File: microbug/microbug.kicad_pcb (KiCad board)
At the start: 2 copper layers, 32.5 x 39.1 mm, 18 parts, among them J1 Conn_01x03, J2 Conn_01x03, M1 Motor_DC, M2 Motor_DC, U1 ATtiny1616-S, U2 QRE1113GR, U3 TC78H651AFNG, U4 QRE1113GR

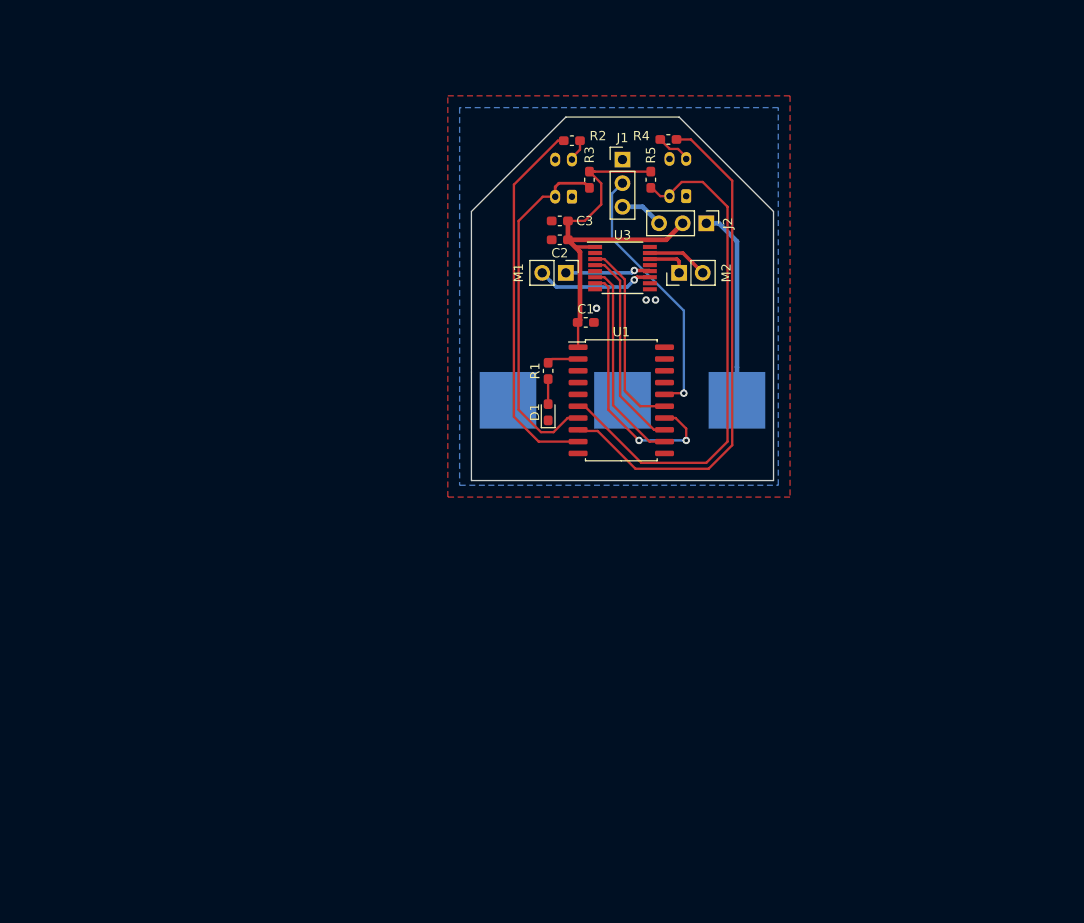
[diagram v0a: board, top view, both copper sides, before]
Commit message: Added more LEDs, changed outline
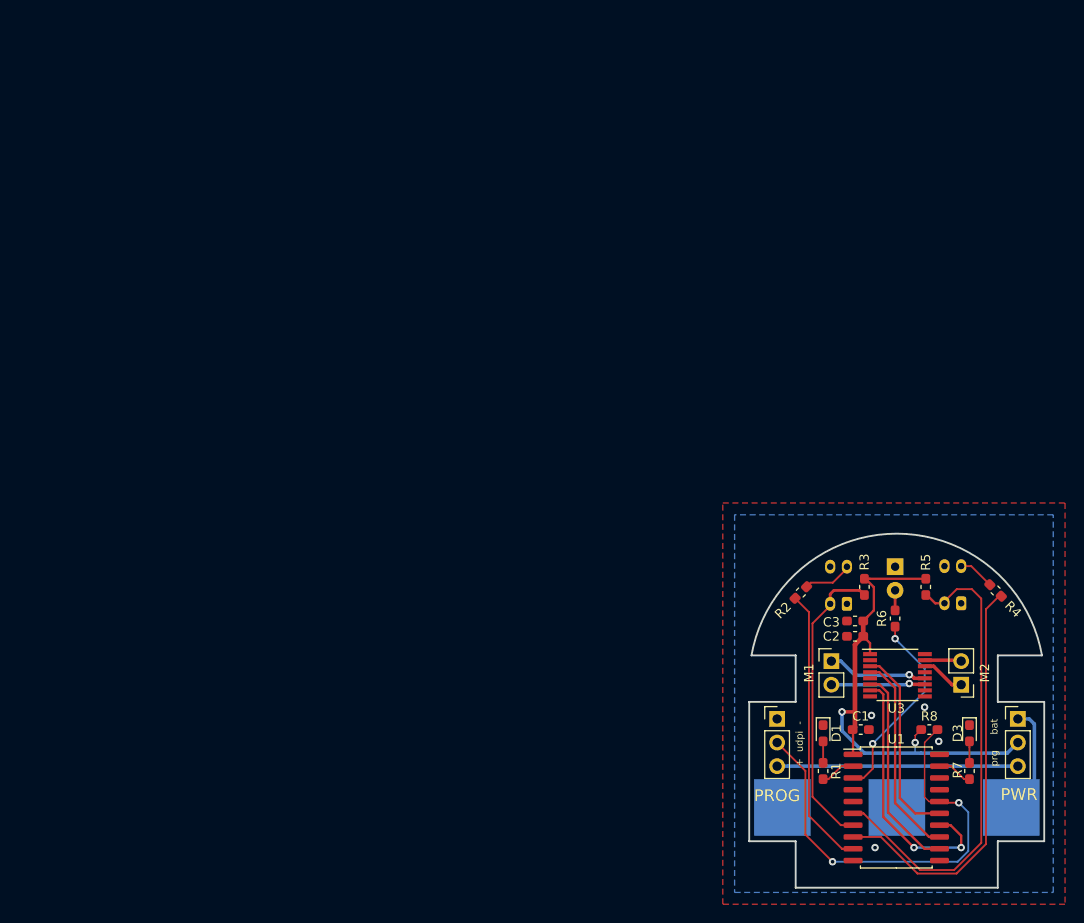
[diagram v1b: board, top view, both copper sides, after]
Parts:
- added D2: LED, LED_THT:LED_D3.0mm, B.Cu at (149.7, 92.6)
- added D3: LED, LED_SMD:LED_0603_1608Metric_Pad1.05x0.95mm_HandSolder, F.Cu at (157.7, 110.5)
- added R6: 220, Resistor_SMD:R_0603_1608Metric_Pad1.05x0.95mm_HandSolder, F.Cu at (149.7, 98.2)
- added R7: 220, Resistor_SMD:R_0603_1608Metric_Pad1.05x0.95mm_HandSolder, F.Cu at (157.7, 114.6)
- added R8: 10k, Resistor_SMD:R_0603_1608Metric_Pad1.05x0.95mm_HandSolder, F.Cu at (153.4, 110.1)
- moved J2 63.0 mm to (162.9, 109.0), turned to 0 degrees
- moved J1 62.5 mm to (137.0, 109.0)
- moved R4 60.0 mm to (160.5, 95.1), turned to 135 degrees
- moved R2 54.5 mm to (139.6, 95.4), turned to 45 degrees
- moved M2 53.7 mm to (156.8, 105.3), turned to 180 degrees
- moved C3 53.5 mm to (145.4, 98.4)
- moved C2 53.2 mm to (145.4, 100.1)
- moved C1 52.9 mm to (146.0, 110.1)
- moved R3 52.9 mm to (146.4, 94.8)
- moved R5 52.9 mm to (153.0, 94.8)
- moved U1 52.9 mm to (149.9, 118.5)
- moved U2 52.9 mm to (144.5, 96.6)
- moved U3 52.9 mm to (150.0, 104.3)
- moved U4 52.9 mm to (156.8, 96.5)
- moved BT1 52.8 mm to (149.9, 118.5)
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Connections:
- net /LED renamed /LED1
- U1 pad 19: Net-(U1-Pad19) -> /LED3
- U1 pad 3: Net-(U1-Pad3) -> /LED2
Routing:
- net /LED2: track 0.00 -> 21.4 mm, vias 0 -> 2
- net Net-(J1-Pad3): track 4.67 -> 25.9 mm
- net /UDPI: track 28.4 -> 47.8 mm, vias 1 -> 2
- net /IR2: track 55.7 -> 44.8 mm
- net +3V3: track 45.6 -> 56.4 mm, vias 0 -> 2
- net /IR1: track 40.3 -> 30.2 mm
- net Net-(BT1-Pad1): track 21.2 -> 12.0 mm
- net /OUT1: track 38.5 -> 32.3 mm
- net /OUT2: track 55.3 -> 51.3 mm
- net /LED3: track 0.00 -> 3.80 mm
- net Net-(R2-Pad2): track 2.39 -> 5.35 mm
- net Net-(M2-Pad2): track 6.57 -> 3.95 mm
- net Net-(M1-Pad2): track 12.7 -> 10.2 mm
- net Net-(D3-Pad2): track 0.00 -> 2.31 mm
- net Net-(D2-Pad2): track 0.00 -> 2.16 mm
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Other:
- board size 32.5 x 39.1 mm -> 31.8 x 38.1 mm
- board text added: "+ udpi -"
- board text added: "PROG"
- board text added: "PWR"
- board text added: "microbug v0"
- board text added: "prg bat"

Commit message: microbug bugging
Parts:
- added G***: LOGO, microbug-fplib:ieee-logo, F.Cu at (85.1, 61.3)
- added J3: Conn_01x02, Connector_PinHeader_2.54mm:PinHeader_1x02_P2.54mm_Vertical, F.Cu at (65.8, 48.0)
- D1, D3: footprint LED_SMD:LED_0603_1608Metric_Pad1.05x0.95mm_HandSolder -> LED_THT:LED_D3.0mm
- M1, M2: footprint Connector_PinHeader_2.54mm:PinHeader_1x02_P2.54mm_Vertical -> microbug-fplib:micro_motor_5mm
- moved U1 97.4 mm to (74.1, 57.3)
- moved R8 97.4 mm to (77.6, 49.0)
- moved C1 97.3 mm to (70.0, 49.5), turned to 180 degrees
- moved J1 94.8 mm to (61.4, 51.8)
- moved J2 94.8 mm to (87.3, 51.8)
- moved BT1 94.6 mm to (74.2, 61.9)
- moved R7 94.3 mm to (77.2, 65.5), turned to 180 degrees
- moved D2 92.0 mm to (74.0, 40.5)
- moved R3 92.0 mm to (70.6, 42.6)
- moved R4 92.0 mm to (84.8, 43.0)
- moved R6 92.0 mm to (74.0, 46.0)
- moved R2 92.0 mm to (63.8, 43.2)
- moved R5 92.0 mm to (77.3, 42.6)
- moved U2 92.0 mm to (68.8, 44.5)
- moved U4 92.0 mm to (81.1, 44.4)
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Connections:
- net Net-(U1-Pad17) renamed /SDA
- net Net-(U1-Pad18) renamed /SCL
- J1 pad 2: /UDPI -> Net-(J1-Pad2)
- J1 pad 3: Net-(J1-Pad3) -> /UDPI
- J2 pad 3: Net-(J1-Pad3) -> Net-(J1-Pad2)
- U1 pad 10: Net-(U1-Pad10) -> /LED1
- U1 pad 11: Net-(U1-Pad11) -> /LED3
- U1 pad 19: /LED3 -> Net-(U1-Pad19)
- U1 pad 2: /LED1 -> Net-(U1-Pad2)
- U1 pad 4: Net-(U1-Pad4) -> /DAC
- U3 pad 11: Net-(M1-Pad2) -> Net-(M1-Pad1)
- U3 pad 12: Net-(M1-Pad1) -> Net-(M1-Pad2)
- U3 pad 14: Net-(M2-Pad1) -> Net-(M2-Pad2)
- U3 pad 15: Net-(M2-Pad2) -> Net-(M2-Pad1)
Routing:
- net /OUT2: track 51.3 -> 20.2 mm
- net Net-(J1-Pad2): track 0.00 -> 28.5 mm, vias 0 -> 1
- net Net-(J1-Pad3): track 25.9 -> 0.00 mm
- net /UDPI: track 47.8 -> 25.7 mm, vias 2 -> 1
- net +3V3: track 56.4 -> 78.0 mm
- net /IR2: track 44.8 -> 27.1 mm
- net Net-(M2-Pad2): track 3.95 -> 20.6 mm
- net /DIR1: track 28.6 -> 13.8 mm, vias 2 -> 0
- net Net-(M2-Pad1): track 4.73 -> 18.8 mm
- net /LED2: track 21.4 -> 9.73 mm, vias 2 -> 0
- net Net-(D1-Pad2): track 2.31 -> 13.1 mm, vias 0 -> 1
- net Net-(D3-Pad2): track 2.31 -> 12.9 mm, vias 0 -> 1
- net /PWM1: track 22.3 -> 13.1 mm
- net /IR1: track 30.2 -> 22.4 mm
- net /DAC: track 0.00 -> 7.53 mm
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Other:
- board size 31.8 x 38.1 mm -> 31.7 x 38.1 mm
- board text added: "-"
- board text added: "DAC"
- board text added: "udpi + -"
- board text removed: "+ udpi -"

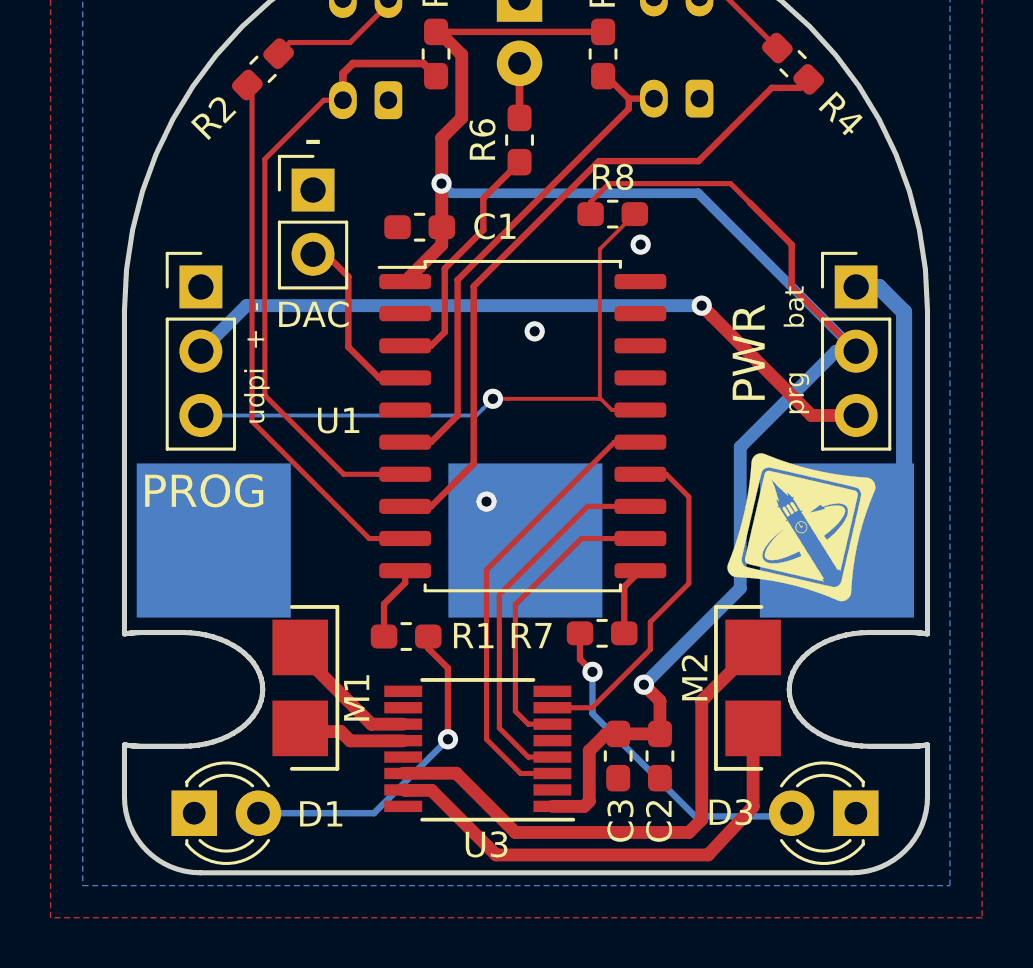
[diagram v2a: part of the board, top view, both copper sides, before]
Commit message: -> kicad v5.99 and added resistor for programming
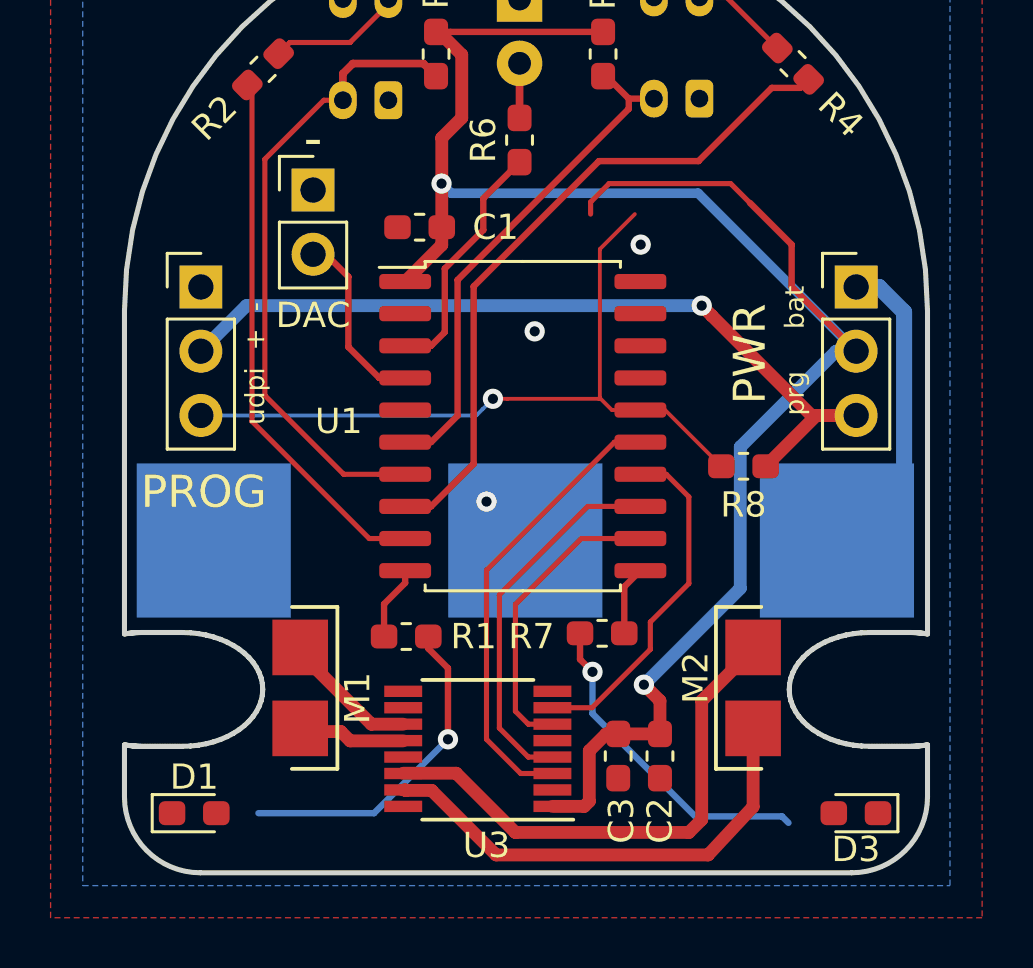
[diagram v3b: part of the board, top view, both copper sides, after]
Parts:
- removed G***: LOGO, microbug-fplib:ieee-logo
- D1, D3: footprint LED_THT:LED_D3.0mm -> LED_SMD:LED_0603_1608Metric_Pad1.05x0.95mm_HandSolder
- R8: value 10k -> 470
- moved R8 11.2 mm to (82.8, 58.9)
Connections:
- R8 pad 1: +3V3 -> /UDPI
- R8 pad 2: /UDPI -> Net-(J1-Pad2)
- U1 pad 19: Net-(U1-Pad19) -> unconnected-(U1-Pad19)
- U1 pad 2: Net-(U1-Pad2) -> unconnected-(U1-Pad2)
- U1 pad 5: Net-(U1-Pad5) -> unconnected-(U1-Pad5)
- U2 pad 1: GND -> Net-(R2-Pad2)
- U2 pad 2: Net-(R2-Pad2) -> GND
- U3 pad 10: Net-(U3-Pad10) -> unconnected-(U3-Pad10)
- U3 pad 13: Net-(U3-Pad13) -> unconnected-(U3-Pad13)
- U3 pad 16: Net-(U3-Pad16) -> unconnected-(U3-Pad16)
- U3 pad 2: Net-(U3-Pad2) -> unconnected-(U3-Pad2)
- U3 pad 5: Net-(U3-Pad5) -> unconnected-(U3-Pad5)
- U3 pad 8: Net-(U3-Pad8) -> unconnected-(U3-Pad8)
- U4 pad 1: GND -> Net-(R4-Pad2)
- U4 pad 2: Net-(R4-Pad2) -> GND
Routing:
- net Net-(J1-Pad2): track 28.5 -> 32.9 mm
- net /UDPI: track 25.7 -> 29.9 mm
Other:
- net class Default removed

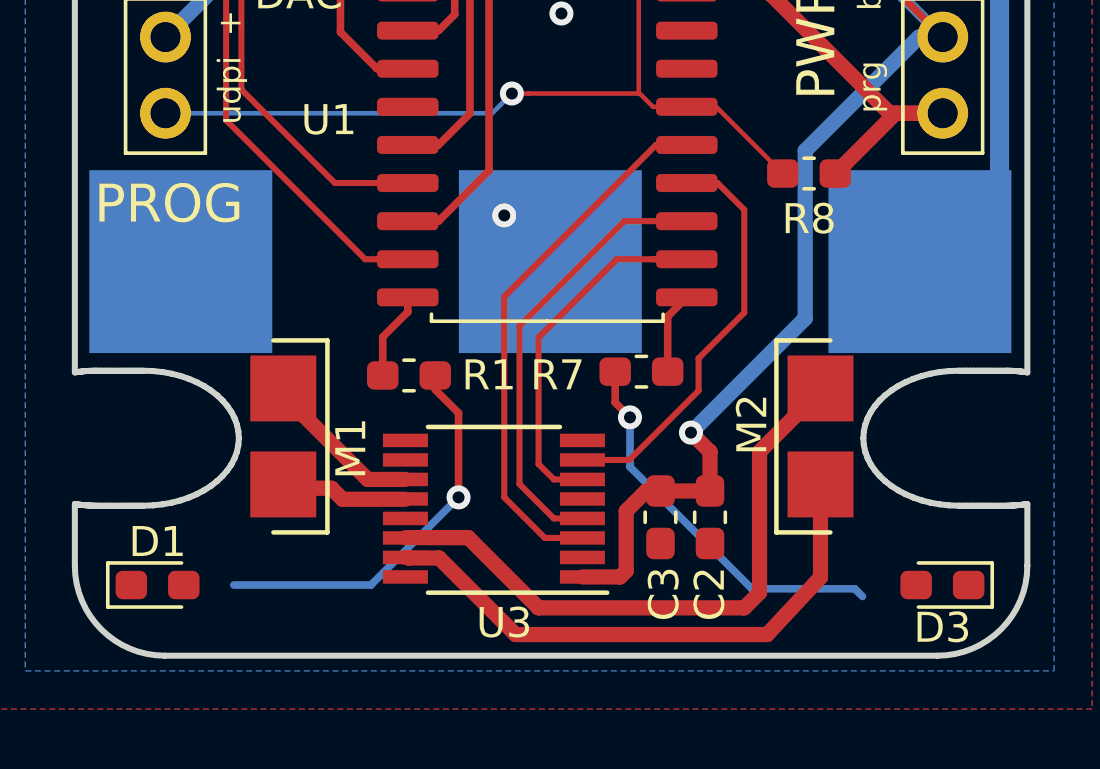
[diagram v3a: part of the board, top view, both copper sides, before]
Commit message: switched driver ic for 660
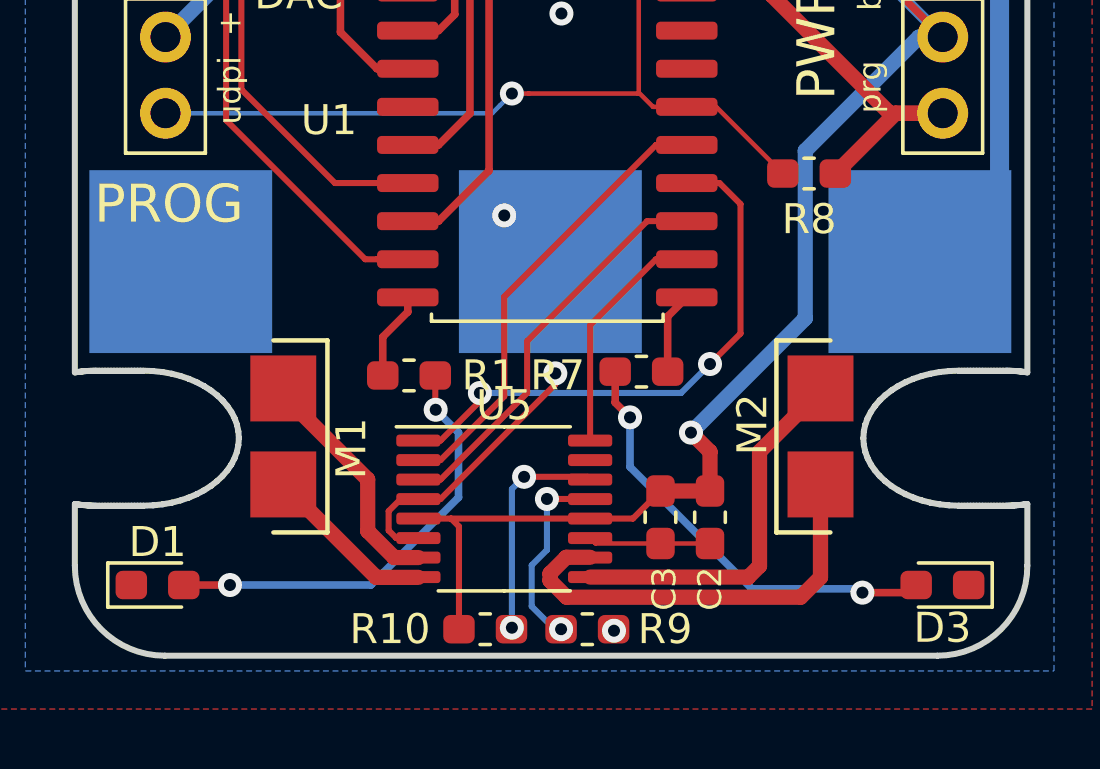
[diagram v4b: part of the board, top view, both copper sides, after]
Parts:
- removed U3: TC78H651AFNG, Package_SO:TSSOP-16_4.4x5mm_P0.65mm
- added R10: 10k, Resistor_SMD:R_0603_1608Metric_Pad1.05x0.95mm_HandSolder, F.Cu at (72.0, 74.1)
- added R9: 47k, Resistor_SMD:R_0603_1608Metric_Pad1.05x0.95mm_HandSolder, F.Cu at (75.4, 74.1)
- added U5: TC78H651AFNG, Package_SO:TSSOP-16_4.4x5mm_P0.65mm, F.Cu at (72.6, 70.1)
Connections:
- U1 pad 12: /PWM1 -> /PWM2
- U1 pad 13: /PWM2 -> /PWM1
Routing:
- net GND: track 0.00 -> 19.1 mm, vias 3 -> 5
- net Net-(U5-Pad9): track 20.6 -> 12.6 mm
- net /PWM2: track 15.9 -> 7.98 mm
- net Net-(R10-Pad2): track 0.00 -> 7.49 mm, vias 0 -> 2
- net +3V3: track 78.0 -> 85.3 mm
- net Net-(R9-Pad2): track 0.00 -> 6.53 mm, vias 0 -> 2
- net Net-(R2-Pad2): track 5.35 -> 0.00 mm
- net /DIR1: track 13.8 -> 18.8 mm, vias 0 -> 2
- net Net-(U5-Pad10): track 18.8 -> 14.4 mm
- net /DIR2: track 18.9 -> 16.1 mm
- net Net-(U5-Pad7): track 5.33 -> 7.85 mm
- net Net-(D3-Pad2): track 12.9 -> 14.9 mm, vias 1 -> 2
- net Net-(D1-Pad2): track 13.1 -> 14.8 mm, vias 1 -> 2
- net Net-(U5-Pad8): track 4.22 -> 5.79 mm

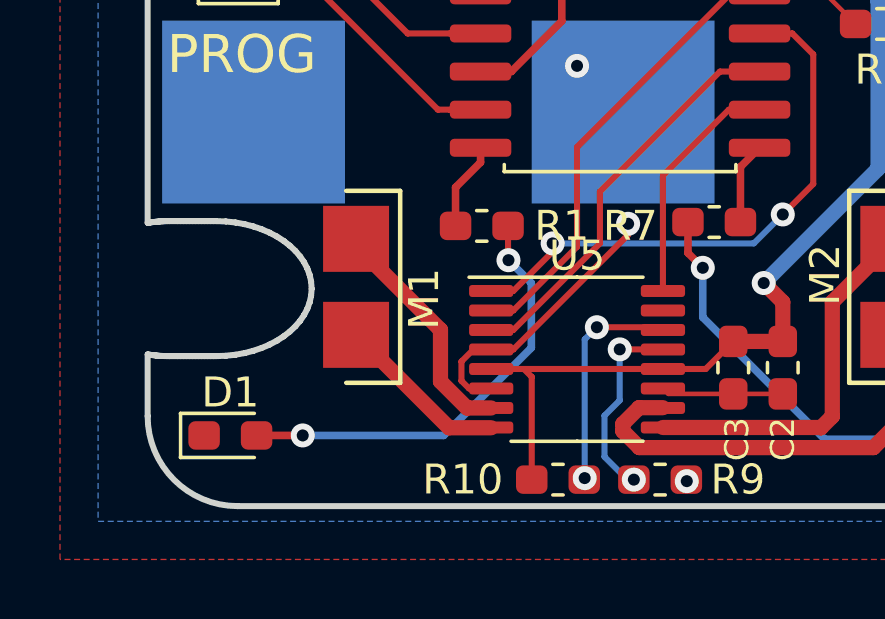
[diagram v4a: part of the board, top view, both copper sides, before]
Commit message: silkscreen stuff and added a via to connect ground planes
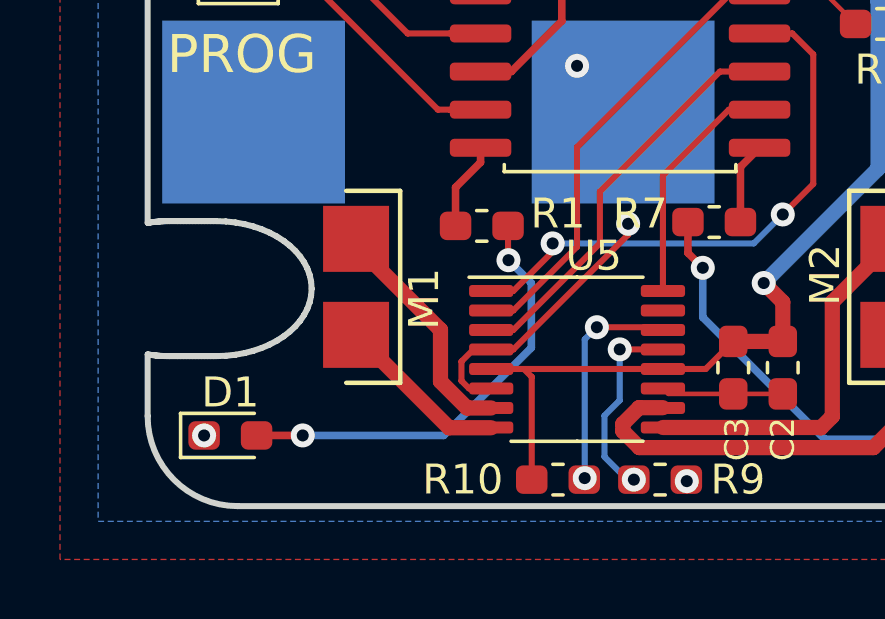
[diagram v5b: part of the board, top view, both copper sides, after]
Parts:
- U5: value TC78H651AFNG -> TC78H660FNG
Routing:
- net Net-(R2-Pad2): track 0.00 -> 5.35 mm
- net GND: track 19.1 -> 13.8 mm, vias 5 -> 6
